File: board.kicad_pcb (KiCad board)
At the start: 6 copper layers, 197 x 139 mm, 36 parts, among them J2 Conn_2Rows-33Pins, J3 Conn_2Rows-33Pins, J4 Conn_2Rows-33Pins, J5 Conn_2Rows-33Pins, J6 Conn_2Rows-33Pins, U1 MC68060RC50, U10 74LVC162245ADGG, U11 74LVC162245ADGG, U2 XC95144XL-5TQG100C, U3 SST39VF1601C-70-4C-EKE, U4 IS61WV51216BLL-10TLI, U5 IS61WV51216BLL-10TLI, U6 SST39VF1601C-70-4C-EKE, U7 74LVC162245ADGG, U8 74LVC162245ADGG, U9 74LVC162245ADGG

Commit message: Added clock chip
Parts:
- added ?: , , F.Cu at (83.5, 87.0)
- added ?: , , F.Cu at (85.0, 87.0)
- added U12: SIT2001BI-S2-33E-50.000000G, Clock:SOT_SiT1630-S_SIT, F.Cu at (84.3, 83.8)
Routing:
- net /GND: track 74.4 -> 99.3 mm, vias 10 -> 18
- net /VCC: track 67.7 -> 87.4 mm, vias 6 -> 14
- net /U1B-CLK: track 23.2 -> 41.1 mm

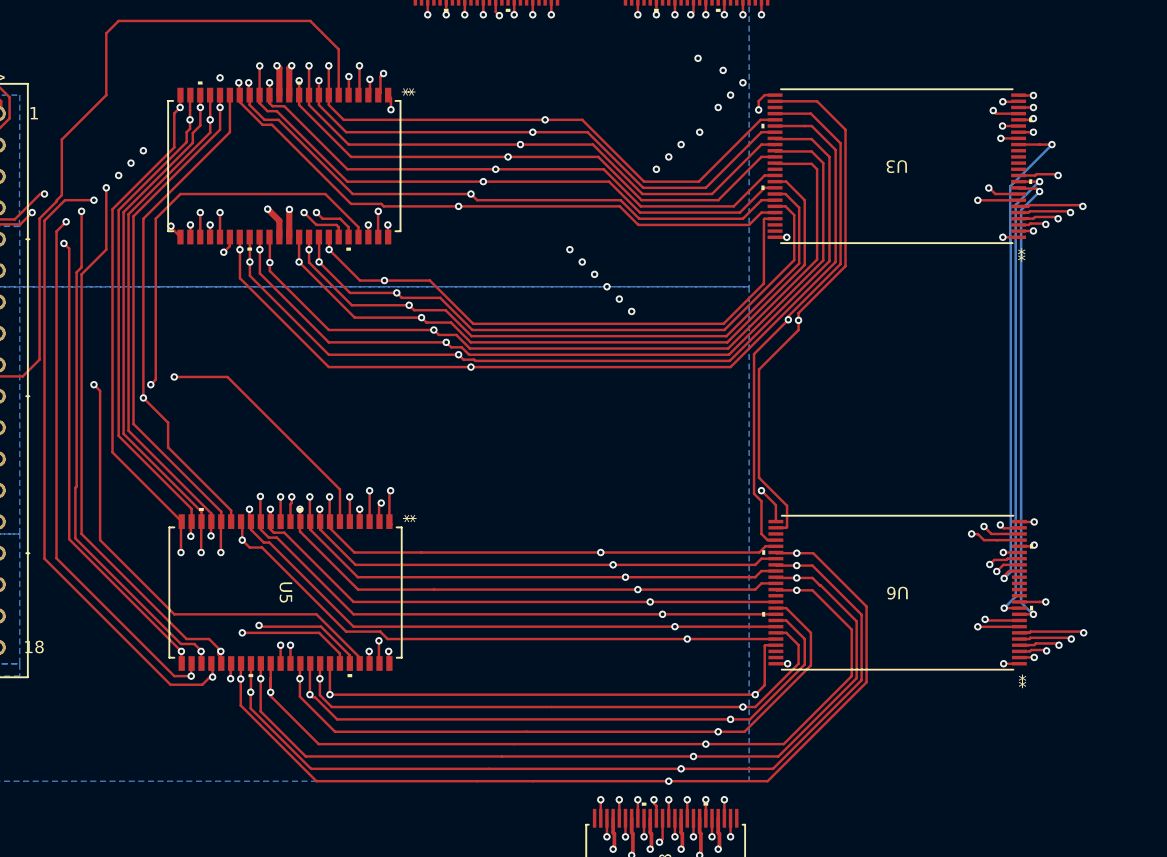
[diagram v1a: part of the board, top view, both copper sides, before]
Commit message: Added A20 to eproms
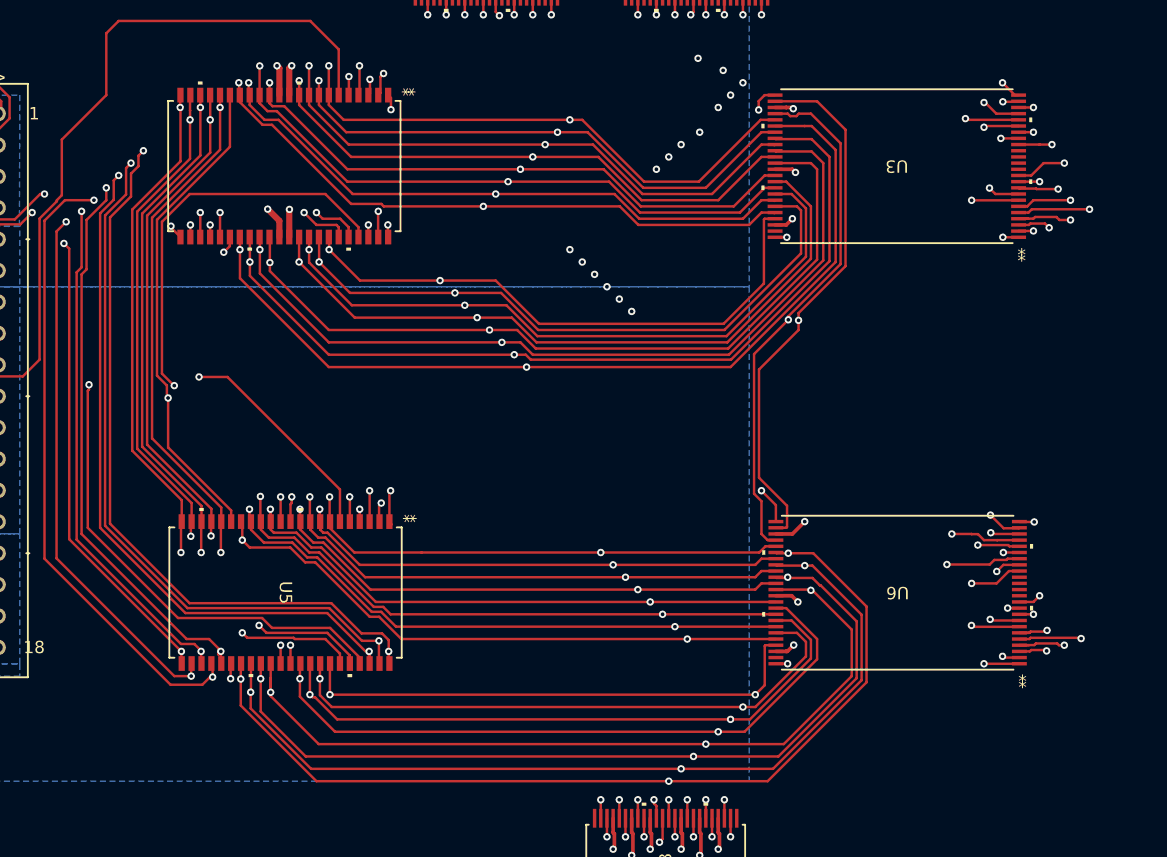
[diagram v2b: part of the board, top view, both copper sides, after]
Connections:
- U3 pad 10: unconnected-(U3-NC-Pad10) -> /A20
- U6 pad 10: unconnected-(U6-NC-Pad10) -> /A20
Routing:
- net /A17: track 288.1 -> 309.2 mm
- net /A15: track 296.2 -> 314.9 mm
- net /A16: track 256.9 -> 275.5 mm
- net /GND: track 99.3 -> 106.8 mm, vias 18 -> 22
- net /A18: track 231.6 -> 238.6 mm
- net /A19: track 244.4 -> 250.5 mm
- net /A5: track 242.4 -> 236.4 mm
- net /A20: track 230.2 -> 235.6 mm
- net /A11: track 293.5 -> 298.9 mm
- net /VCC: track 87.4 -> 91.2 mm, vias 14 -> 16
- net /A10: track 302.5 -> 306.2 mm
- net /A4: track 216.7 -> 219.9 mm
- net /A12: track 288.5 -> 291.5 mm
- net /A3: track 226.4 -> 229.2 mm
- net /A14: track 321.3 -> 319.0 mm
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
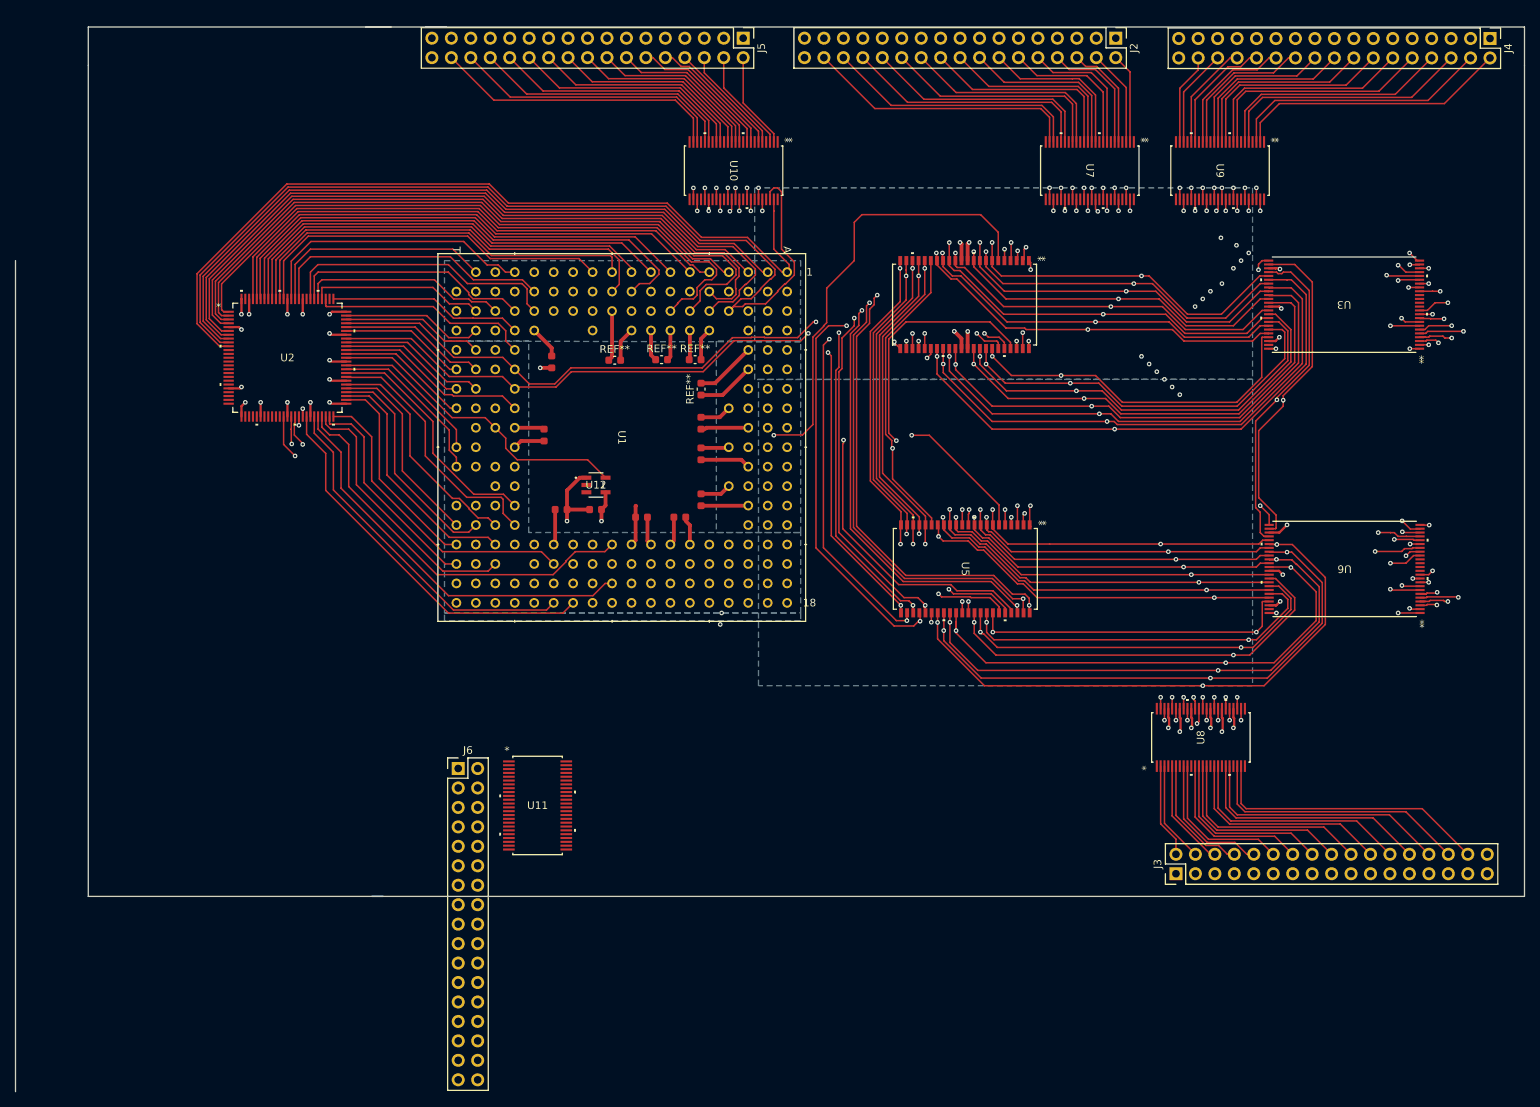
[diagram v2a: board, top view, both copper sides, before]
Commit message: Added ext bus control lines
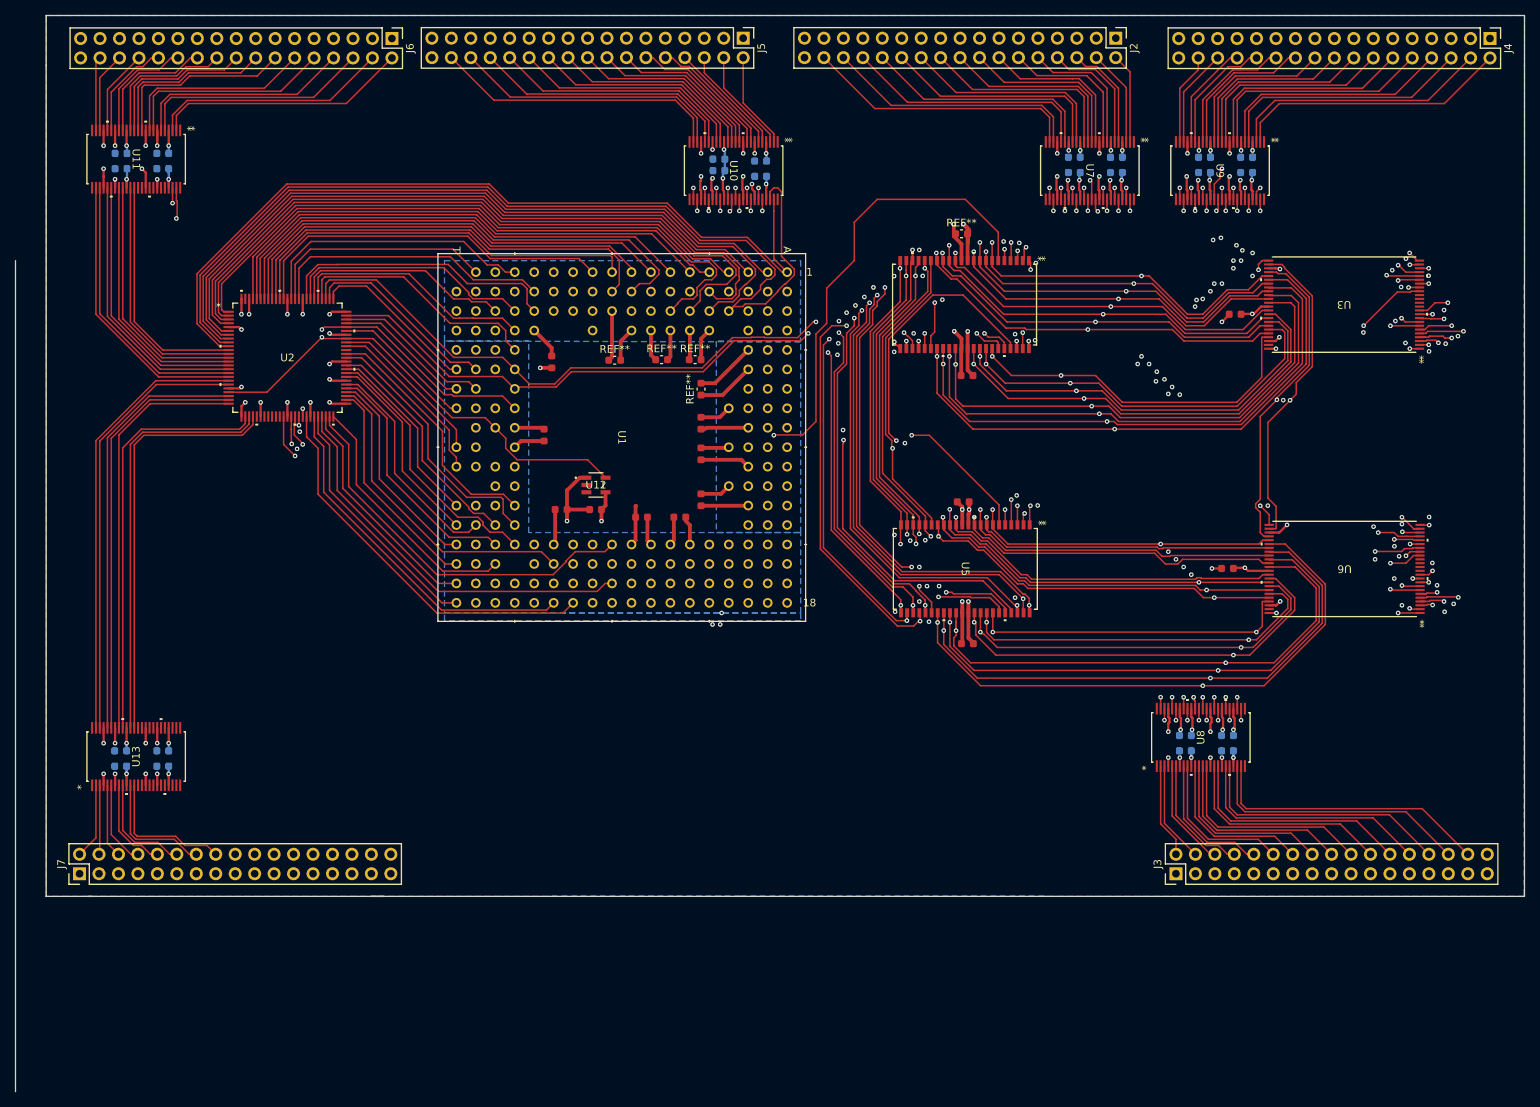
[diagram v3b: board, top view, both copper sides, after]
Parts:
- added ?: , , F.Cu at (21.5, 42.5)
- added ?: , , F.Cu at (168.5, 61.5)
- added ?: , , F.Cu at (164.5, 43.0)
- added ?: , , F.Cu at (26.9, 42.5)
- added ?: , , F.Cu at (160.4, 116.5)
- added ?: , , F.Cu at (165.9, 116.5)
- added ?: , , F.Cu at (23.0, 118.5)
- added ?: , , F.Cu at (162.9, 43.0)
- added ?: , , F.Cu at (162.0, 118.5)
- added ?: , , F.Cu at (131.9, 69.5)
- added ?: , , F.Cu at (167.5, 116.5)
- added ?: , , F.Cu at (105.0, 41.5)
- added ?: , , F.Cu at (145.9, 43.0)
- added ?: , , F.Cu at (160.4, 118.5)
- added ?: , , F.Cu at (101.1, 42.8)
- added ?: , , F.Cu at (133.5, 69.5)
- added ?: , , F.Cu at (170.0, 43.0)
- added ?: , , F.Cu at (167.5, 118.5)
- added ?: , , F.Cu at (147.5, 41.0)
- added ?: , , F.Cu at (21.4, 118.5)
- added ?: , , F.Cu at (165.9, 94.7)
- added ?: , , F.Cu at (23.1, 42.5)
- added ?: , , F.Cu at (167.5, 94.7)
- added ?: , , F.Cu at (151.4, 41.0)
- added ?: , , F.Cu at (153.0, 43.0)
- added ?: , , F.Cu at (147.5, 43.0)
- added ?: , , F.Cu at (168.4, 43.0)
- added ?: , , F.Cu at (106.5, 41.5)
- added ?: , , F.Cu at (106.5, 43.5)
- added ?: , , F.Cu at (151.4, 43.0)
- added ?: , , F.Cu at (26.9, 40.5)
- added ?: , , F.Cu at (21.4, 120.5)
- added ?: , , F.Cu at (28.5, 42.5)
- added ?: , , F.Cu at (23.1, 40.5)
- added ?: , , F.Cu at (166.9, 61.5)
- added ?: , , F.Cu at (162.9, 41.0)
- added ?: , , F.Cu at (131.4, 86.0)
- added ?: , , F.Cu at (28.5, 40.5)
- added ?: , , F.Cu at (132.0, 104.5)
- added ?: , , F.Cu at (133.0, 86.0)
- added ?: , , F.Cu at (105.0, 43.5)
- added ?: , , F.Cu at (28.5, 118.5)
- added ?: , , F.Cu at (26.9, 120.5)
- added ?: , , F.Cu at (21.5, 40.5)
- added ?: , , F.Cu at (133.6, 104.5)
- added ?: , , F.Cu at (164.5, 41.0)
- added ?: , , F.Cu at (101.1, 41.2)
- added ?: , , F.Cu at (153.0, 41.0)
- added ?: , , F.Cu at (99.5, 42.8)
- added ?: , , F.Cu at (145.9, 41.0)
- added ?: , , F.Cu at (168.4, 41.0)
- added ?: , , F.Cu at (170.0, 41.0)
- added ?: , , F.Cu at (23.0, 120.5)
- added ?: , , F.Cu at (162.0, 116.5)
- added ?: , , F.Cu at (99.5, 41.2)
- added ?: , , F.Cu at (165.9, 118.5)
- added ?: , , F.Cu at (28.5, 120.5)
- added ?: , , F.Cu at (26.9, 118.5)
- added J7: Conn_2Rows-33Pins, Connector_PinHeader_2.54mm:PinHeader_2x17_P2.54mm_Vertical, F.Cu at (16.9, 134.5)
- added REF**: C_0603_1608Metric, Capacitor_SMD:C_0603_1608Metric, F.Cu at (132.0, 51.0)
- added U13: 74LVC162245ADGG, 74 buffer:SOT362-1_NEX, F.Cu at (24.3, 119.2)
- moved U11 99.3 mm to (24.3, 41.2), turned to -90 degrees
- moved J6 95.7 mm to (57.6, 25.5), turned to -90 degrees
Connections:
- J6 pad 1: unconnected-(J6-Pin_1-Pad1) -> /GND
- J6 pad 10: unconnected-(J6-Pin_10-Pad10) -> /EXT_CTRLOUT4
- J6 pad 11: unconnected-(J6-Pin_11-Pad11) -> /GND
- J6 pad 12: unconnected-(J6-Pin_12-Pad12) -> /EXT_CTRLOUT5
- J6 pad 13: unconnected-(J6-Pin_13-Pad13) -> /GND
- J6 pad 14: unconnected-(J6-Pin_14-Pad14) -> /EXT_CTRLOUT6
- J6 pad 15: unconnected-(J6-Pin_15-Pad15) -> /GND
- J6 pad 16: unconnected-(J6-Pin_16-Pad16) -> /EXT_CTRLOUT7
- J6 pad 17: unconnected-(J6-Pin_17-Pad17) -> /GND
- J6 pad 18: unconnected-(J6-Pin_18-Pad18) -> /EXT_CTRLOUT8
- J6 pad 19: unconnected-(J6-Pin_19-Pad19) -> /GND
- J6 pad 2: unconnected-(J6-Pin_2-Pad2) -> /EXT_CTRLOUT0
- J6 pad 20: unconnected-(J6-Pin_20-Pad20) -> /EXT_CTRLOUT9
- J6 pad 21: unconnected-(J6-Pin_21-Pad21) -> /GND
- J6 pad 22: unconnected-(J6-Pin_22-Pad22) -> /EXT_CTRLOUT10
- J6 pad 23: unconnected-(J6-Pin_23-Pad23) -> /GND
- J6 pad 24: unconnected-(J6-Pin_24-Pad24) -> /EXT_CTRLOUT11
- J6 pad 25: unconnected-(J6-Pin_25-Pad25) -> /GND
- J6 pad 26: unconnected-(J6-Pin_26-Pad26) -> /EXT_CTRLOUT12
- J6 pad 27: unconnected-(J6-Pin_27-Pad27) -> /GND
- J6 pad 28: unconnected-(J6-Pin_28-Pad28) -> /EXT_CTRLOUT13
- J6 pad 29: unconnected-(J6-Pin_29-Pad29) -> /GND
- J6 pad 3: unconnected-(J6-Pin_3-Pad3) -> /GND
- J6 pad 30: unconnected-(J6-Pin_30-Pad30) -> /EXT_CTRLOUT14
- J6 pad 31: unconnected-(J6-Pin_31-Pad31) -> /GND
- J6 pad 32: unconnected-(J6-Pin_32-Pad32) -> /EXT_CTRLOUT15
- J6 pad 33: unconnected-(J6-Pin_33-Pad33) -> /GND
- J6 pad 4: unconnected-(J6-Pin_4-Pad4) -> /EXT_CTRLOUT1
- J6 pad 5: unconnected-(J6-Pin_5-Pad5) -> /GND
- J6 pad 6: unconnected-(J6-Pin_6-Pad6) -> /EXT_CTRLOUT2
- J6 pad 7: unconnected-(J6-Pin_7-Pad7) -> /GND
- J6 pad 8: unconnected-(J6-Pin_8-Pad8) -> /EXT_CTRLOUT3
- J6 pad 9: unconnected-(J6-Pin_9-Pad9) -> /GND
- U1 pad Q11: unconnected-(U1C-*BGR-PadQ11) -> /U1C-BGR
- U1 pad Q15: unconnected-(U1C-*BTT-PadQ15) -> /U1C-BTT
- U1 pad T13: unconnected-(U1C-*BG-PadT13) -> /U1C-BG
- U1 pad T17: unconnected-(U1C-*BB-PadT17) -> /U1C-BB
- U1 pad T18: unconnected-(U1C-*BR-PadT18) -> /U1C-BR
- U10 pad 10: unconnected-(U10-GND-Pad10) -> /GND
- U10 pad 15: unconnected-(U10-GND-Pad15) -> /GND
- U10 pad 18: unconnected-(U10-VCC-Pad18) -> /VCC
- U10 pad 21: unconnected-(U10-GND-Pad21) -> /GND
- U10 pad 28: unconnected-(U10-GND-Pad28) -> /GND
- U10 pad 31: unconnected-(U10-VCC-Pad31) -> /VCC
- U10 pad 34: unconnected-(U10-GND-Pad34) -> /GND
- U10 pad 39: unconnected-(U10-GND-Pad39) -> /GND
- U10 pad 4: unconnected-(U10-GND-Pad4) -> /GND
- U10 pad 42: unconnected-(U10-VCC-Pad42) -> /VCC
- U10 pad 45: unconnected-(U10-GND-Pad45) -> /GND
- U10 pad 7: unconnected-(U10-VCC-Pad7) -> /VCC
- U11 pad 10: unconnected-(U11-GND-Pad10) -> /GND
- U11 pad 11: unconnected-(U11-1B6-Pad11) -> /EXT_CTRLOUT6
- U11 pad 12: unconnected-(U11-1B7-Pad12) -> /EXT_CTRLOUT7
- U11 pad 13: unconnected-(U11-2B0-Pad13) -> /EXT_CTRLOUT8
- U11 pad 14: unconnected-(U11-2B1-Pad14) -> /EXT_CTRLOUT9
- U11 pad 15: unconnected-(U11-GND-Pad15) -> /GND
- U11 pad 16: unconnected-(U11-2B2-Pad16) -> /EXT_CTRLOUT10
- U11 pad 17: unconnected-(U11-2B3-Pad17) -> /EXT_CTRLOUT11
- U11 pad 18: unconnected-(U11-VCC-Pad18) -> /VCC
- U11 pad 19: unconnected-(U11-2B4-Pad19) -> /EXT_CTRLOUT12
- U11 pad 2: unconnected-(U11-1B0-Pad2) -> /EXT_CTRLOUT0
- U11 pad 20: unconnected-(U11-2B5-Pad20) -> /EXT_CTRLOUT13
- U11 pad 21: unconnected-(U11-GND-Pad21) -> /GND
- U11 pad 22: unconnected-(U11-2B6-Pad22) -> /EXT_CTRLOUT14
- U11 pad 23: unconnected-(U11-2B7-Pad23) -> /EXT_CTRLOUT15
- U11 pad 26: unconnected-(U11-2A7-Pad26) -> /CPLD_X7
- U11 pad 27: unconnected-(U11-2A6-Pad27) -> /CPLD_X6
- U11 pad 28: unconnected-(U11-GND-Pad28) -> /GND
- U11 pad 29: unconnected-(U11-2A5-Pad29) -> /CPLD_X5
- U11 pad 3: unconnected-(U11-1B1-Pad3) -> /EXT_CTRLOUT1
- U11 pad 30: unconnected-(U11-2A4-Pad30) -> /CPLD_X4
- U11 pad 31: unconnected-(U11-VCC-Pad31) -> /VCC
- U11 pad 32: unconnected-(U11-2A3-Pad32) -> /CPLD_X3
- U11 pad 33: unconnected-(U11-2A2-Pad33) -> /CPLD_X2
- U11 pad 34: unconnected-(U11-GND-Pad34) -> /GND
- U11 pad 35: unconnected-(U11-2A1-Pad35) -> /CPLD_X1
- U11 pad 36: unconnected-(U11-2A0-Pad36) -> /CPLD_X0
- U11 pad 39: unconnected-(U11-GND-Pad39) -> /GND
- U11 pad 4: unconnected-(U11-GND-Pad4) -> /GND
- U11 pad 42: unconnected-(U11-VCC-Pad42) -> /VCC
- U11 pad 45: unconnected-(U11-GND-Pad45) -> /GND
- U11 pad 46: unconnected-(U11-1A1-Pad46) -> /U1B-CLKEN
- U11 pad 47: unconnected-(U11-1A0-Pad47) -> /U1B-CLK
- U11 pad 5: unconnected-(U11-1B2-Pad5) -> /EXT_CTRLOUT2
- U11 pad 6: unconnected-(U11-1B3-Pad6) -> /EXT_CTRLOUT3
- U11 pad 7: unconnected-(U11-VCC-Pad7) -> /VCC
- U11 pad 8: unconnected-(U11-1B4-Pad8) -> /EXT_CTRLOUT4
- U11 pad 9: unconnected-(U11-1B5-Pad9) -> /EXT_CTRLOUT5
- U2 pad 11: unconnected-(U2-IO-Pad11) -> /CPLD_X0
- U2 pad 12: unconnected-(U2-IO-Pad12) -> /CPLD_X1
- U2 pad 13: unconnected-(U2-IO-Pad13) -> /CPLD_X2
- U2 pad 14: unconnected-(U2-IO-Pad14) -> /CPLD_X3
- U2 pad 15: unconnected-(U2-IO-Pad15) -> /CPLD_X4
- U2 pad 16: unconnected-(U2-IO-Pad16) -> /CPLD_X5
- U2 pad 17: unconnected-(U2-IO-Pad17) -> /CPLD_X6
- U2 pad 18: unconnected-(U2-IO-Pad18) -> /CPLD_X7
- U2 pad 19: unconnected-(U2-IO-Pad19) -> /CPLD_XIN0
- U2 pad 20: unconnected-(U2-IO-Pad20) -> /CPLD_XIN1
- U2 pad 22: unconnected-(U2-I/O/GCK1-Pad22) -> /U1B-CLK
- U2 pad 23: unconnected-(U2-I/O/GCK2-Pad23) -> /CPLD_XIN2
- U2 pad 24: unconnected-(U2-IO-Pad24) -> /CPLD_XIN3
- U2 pad 25: unconnected-(U2-IO-Pad25) -> /CPLD_XIN4
- U2 pad 27: unconnected-(U2-I/O/GCK3-Pad27) -> /CPLD_XIN5
- U2 pad 28: unconnected-(U2-IO-Pad28) -> /CPLD_XIN6
- U2 pad 29: unconnected-(U2-IO-Pad29) -> /CPLD_XIN7
- U2 pad 46: /U1C-TM2 -> /U1C-BR
- U2 pad 47: /U1C-CLA -> /U1C-TM2
- U2 pad 48: /U1C-TS -> /U1C-BB
- U2 pad 49: /U1C-PST3 -> /U1C-CLA
- U2 pad 50: /U1C-RW -> /U1C-TS
- U2 pad 52: /U1C-PST0 -> /U1C-PST3
- U2 pad 53: /U1C-TIP -> /U1C-RW
- U2 pad 54: /U1C-PST1 -> /U1C-PST0
- U2 pad 55: /U1C-TA -> /U1C-TIP
- U2 pad 56: /U1C-PST2 -> /U1C-PST1
- U2 pad 58: /U1C-SAS -> /U1C-TA
- U2 pad 59: /U1C-PST4 -> /U1C-BTT
- U2 pad 60: /U1C-AVEC -> /U1C-BG
- U2 pad 61: /U1C-TCI -> /U1C-PST2
- U2 pad 63: /U1B-CLK -> /U1C-SAS
- U2 pad 64: /U1B-IPL0 -> /U1C-PST4
- U2 pad 65: /U1B-CLKEN -> /U1C-BGR
- U2 pad 66: /U1B-IPL1 -> /U1C-AVEC
- U2 pad 67: /U1B-RSTI -> /U1C-TCI
- U2 pad 68: /BS3 -> /U1B-CLK
- U2 pad 70: /U1B-IPL2 -> /U1B-IPL0
- U2 pad 71: /U1B-MDIS -> /U1B-CLKEN
- U2 pad 72: /BS2 -> /U1B-IPL1
- U2 pad 73: /U1B-TMS -> /U1B-RSTI
- U2 pad 74: /U1B-TCK -> /BS3
- U2 pad 76: /BS0 -> /U1B-IPL2
- U2 pad 77: unconnected-(U2-NC-Pad77) -> /U1B-MDIS
- U2 pad 78: /BS1 -> /BS2
- U2 pad 79: /U1B-TDI -> /BS1
- U2 pad 80: /U1B-RSTO -> /BS0
- U2 pad 81: /U1B-UPA0 -> /U1B-RSTO
- U2 pad 82: /U1A-TT0 -> /U1B-UPA0
- U2 pad 83: /U1B-TD0 -> /U1A-TT0
- U3 pad 10: /A20 -> unconnected-(U3-NC-Pad10)
- U6 pad 10: /A20 -> unconnected-(U6-NC-Pad10)
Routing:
- net /GND: track 106.8 -> 229.8 mm, vias 22 -> 136
- net /CPLD_XIN0: track 0.00 -> 58.1 mm
- net /CPLD_XIN1: track 0.00 -> 57.3 mm
- net /VCC: track 91.2 -> 148.3 mm, vias 16 -> 39
- net /CPLD_XIN2: track 0.00 -> 56.0 mm
- net /CPLD_XIN3: track 0.00 -> 55.2 mm
- net /CPLD_XIN5: track 0.00 -> 54.8 mm
- net /CPLD_XIN6: track 0.00 -> 54.6 mm
- net /CPLD_XIN7: track 0.00 -> 54.6 mm
- net /CPLD_XIN4: track 0.00 -> 54.3 mm
- net /U1B-CLK: track 41.1 -> 90.1 mm, vias 0 -> 2
- net /A18: track 238.6 -> 278.6 mm, vias 5 -> 7
- net /CPLD_X7: track 0.00 -> 37.2 mm
- net /CPLD_X6: track 0.00 -> 36.5 mm
- net /CPLD_X5: track 0.00 -> 35.5 mm
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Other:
- board size 197 x 139 mm -> 197 x 140.5 mm
